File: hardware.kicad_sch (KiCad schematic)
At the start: 11 parts, among them J2 MDT320B03001, P1 USB_C_Plug, U4 CH340C

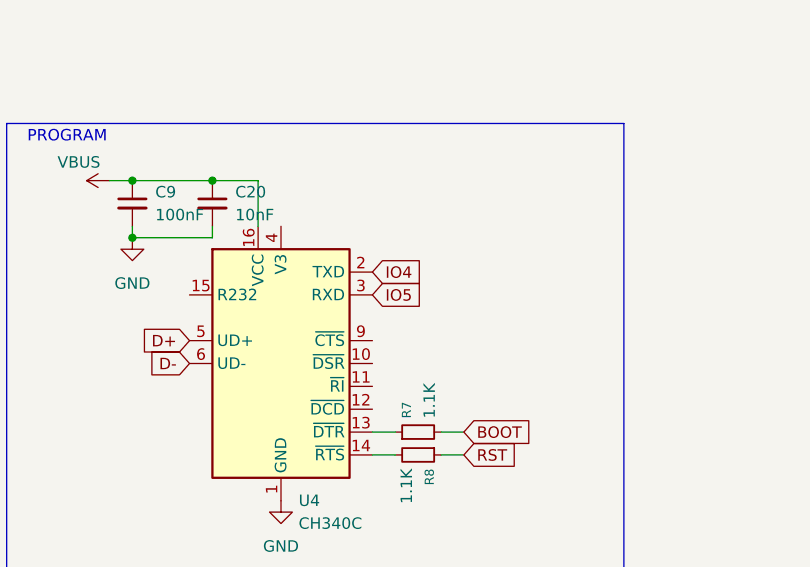
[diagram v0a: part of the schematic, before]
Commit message: switch uart wiring
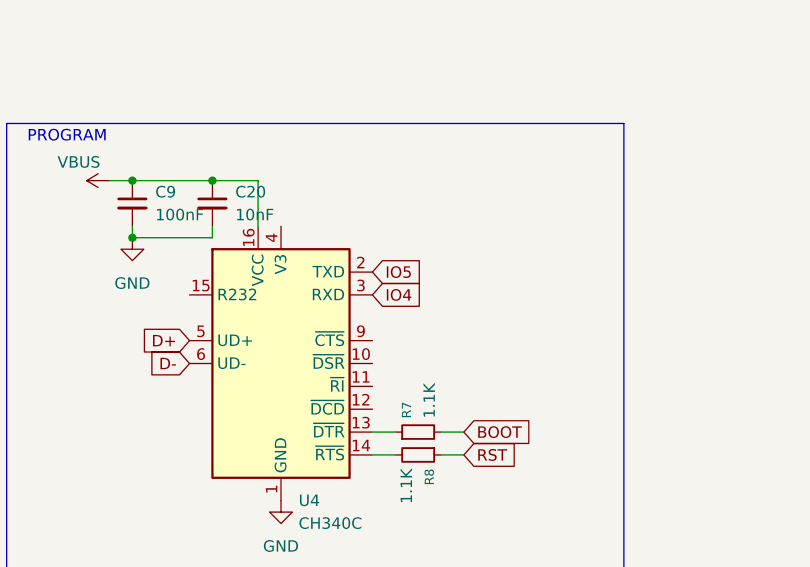
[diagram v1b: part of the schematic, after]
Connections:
- net IO4: now also U4.3 (RXD); no longer U4.2 (TXD)
- net IO5: now also U4.2 (TXD); no longer U4.3 (RXD)

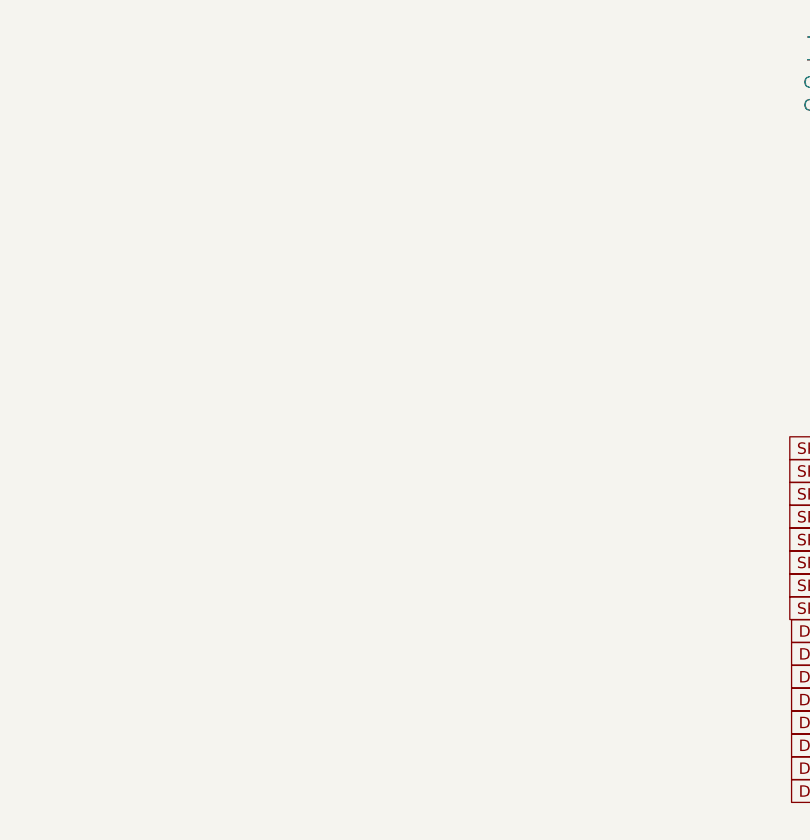
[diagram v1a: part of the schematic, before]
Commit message: add testing header
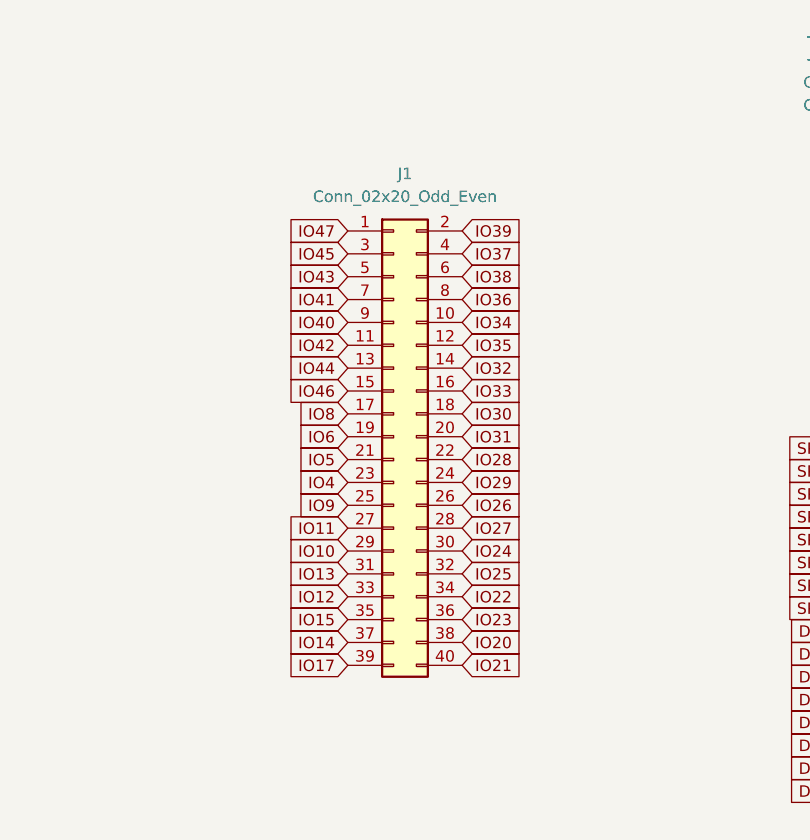
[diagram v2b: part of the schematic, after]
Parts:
- added J1: Conn_02x20_Odd_Even, Connector_IDC:IDC-Header_2x20_P2.54mm_Horizontal, symbol Connector_Generic:Conn_02x20_Odd_Even
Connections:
- net IO10: now also J1.29 (Pin_29)
- net IO11: now also J1.27 (Pin_27)
- net IO12: now also J1.33 (Pin_33)
- net IO13: now also J1.31 (Pin_31)
- net IO14: now also J1.37 (Pin_37)
- net IO15: now also J1.35 (Pin_35)
- net IO17: now also J1.39 (Pin_39)
- net IO20: now also J1.38 (Pin_38)
- net IO21: now also J1.40 (Pin_40)
- net IO22: now also J1.34 (Pin_34)
- net IO23: now also J1.36 (Pin_36)
- net IO24: now also J1.30 (Pin_30)
- net IO25: now also J1.32 (Pin_32)
- net IO26: now also J1.26 (Pin_26)
- net IO27: now also J1.28 (Pin_28)
- net IO28: now also J1.22 (Pin_22)
- net IO29: now also J1.24 (Pin_24)
- net IO30: now also J1.18 (Pin_18)
- net IO31: now also J1.20 (Pin_20)
- net IO32: now also J1.14 (Pin_14)
- net IO33: now also J1.16 (Pin_16)
- net IO34: now also J1.10 (Pin_10)
- net IO35: now also J1.12 (Pin_12)
- net IO36: now also J1.8 (Pin_8)
- net IO37: now also J1.4 (Pin_4)
- net IO38: now also J1.6 (Pin_6)
- net IO39: now also J1.2 (Pin_2)
- net IO4: now also J1.23 (Pin_23)
- net IO40: now also J1.9 (Pin_9)
- net IO41: now also J1.7 (Pin_7)
- net IO42: now also J1.11 (Pin_11)
- net IO43: now also J1.5 (Pin_5)
- net IO44: now also J1.13 (Pin_13)
- net IO45: now also J1.3 (Pin_3)
- net IO46: now also J1.15 (Pin_15)
- net IO47: now also J1.1 (Pin_1)
- net IO5: now also J1.21 (Pin_21)
- net IO6: now also J1.19 (Pin_19)
- net IO8: now also J1.17 (Pin_17)
- net IO9: now also J1.25 (Pin_25)

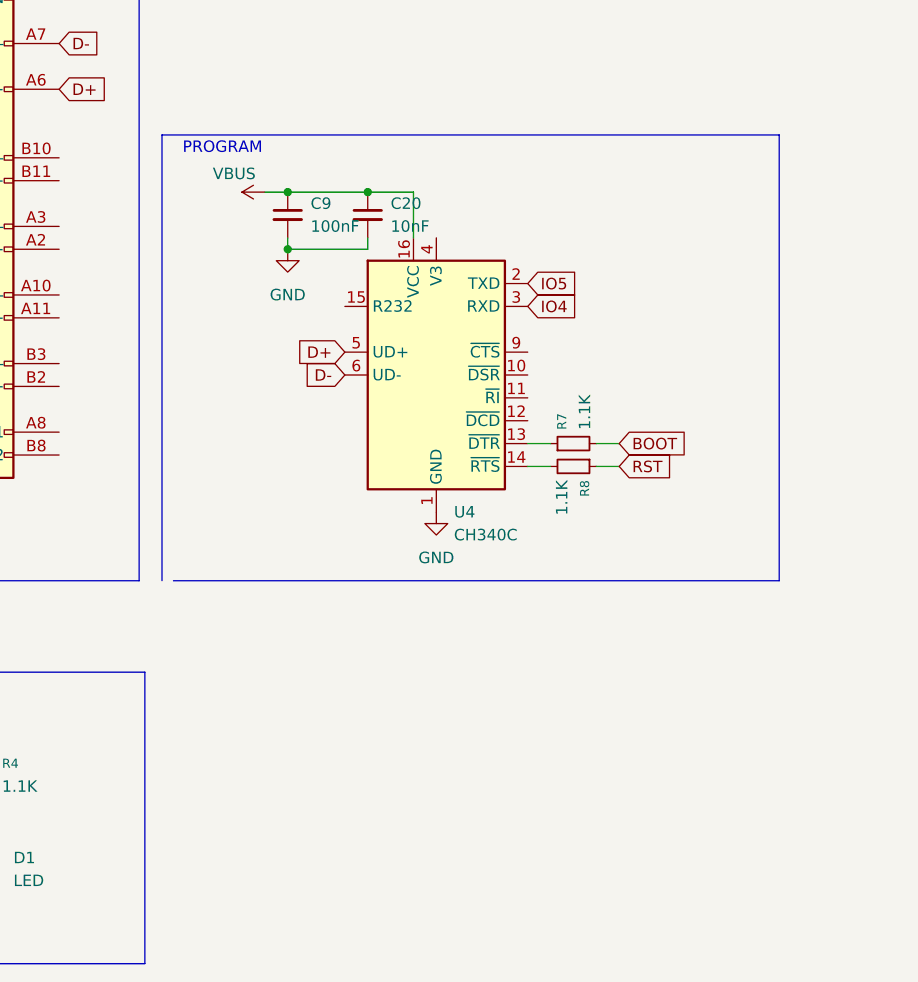
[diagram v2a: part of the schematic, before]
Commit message: add rst/boot pull up
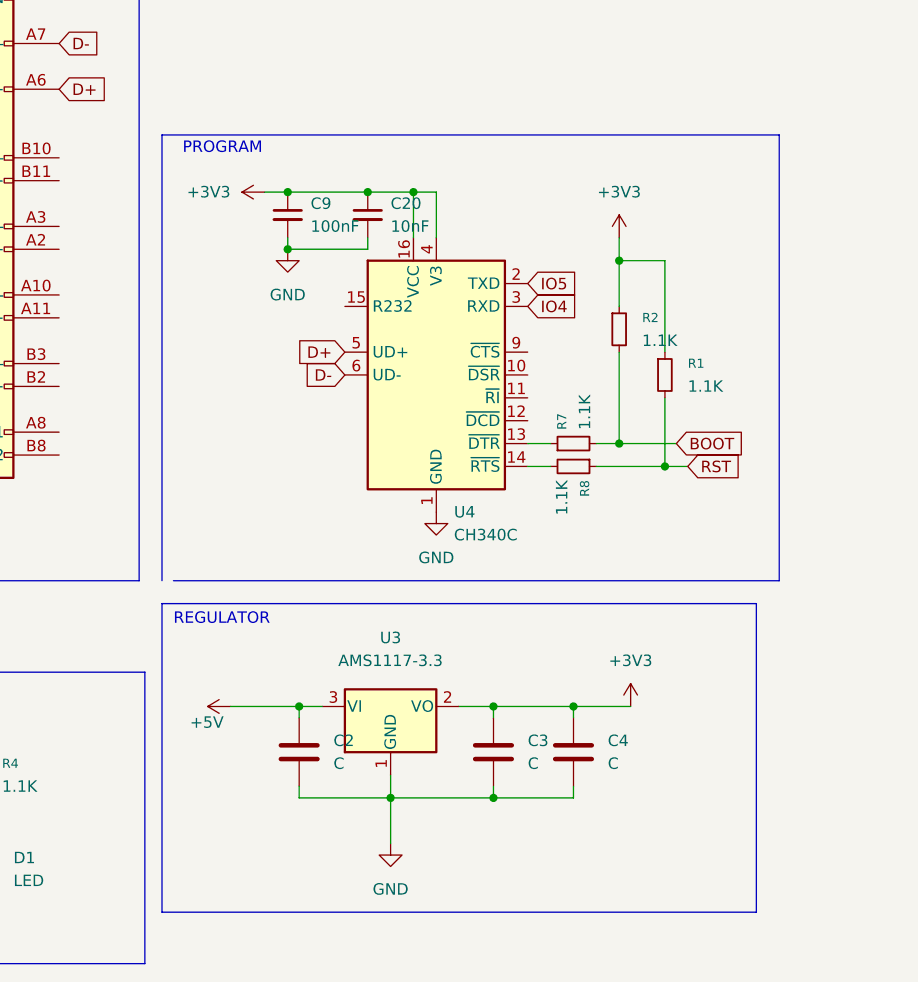
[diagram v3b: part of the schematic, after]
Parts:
- added C2, C3, C4: C, Capacitor_SMD:C_0603_1608Metric, symbol Device:C
- added R1, R2: 1.1K, Resistor_SMD:R_0603_1608Metric, symbol Device:R_Small
- added U3: AMS1117-3.3, Package_TO_SOT_SMD:SOT-223-3_TabPin2, symbol Regulator_Linear:AMS1117-3.3
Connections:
- net +5V: now also C2.1, U3.3 (VI); no longer C20.1, C9.1, U4.16 (VCC)
- net BOOT: now also R2.2
- net GND: now also C2.2, C3.2, C4.2, U3.1 (GND)
- net RST: now also R1.2
- net +3V3: now reaches U4.4 (V3)
- net +3V3: now also C20.1, C9.1, U4.16 (VCC), C3.1, C4.1, R1.1, R2.1, U3.2 (VO)
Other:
- note added: "REGULATOR"

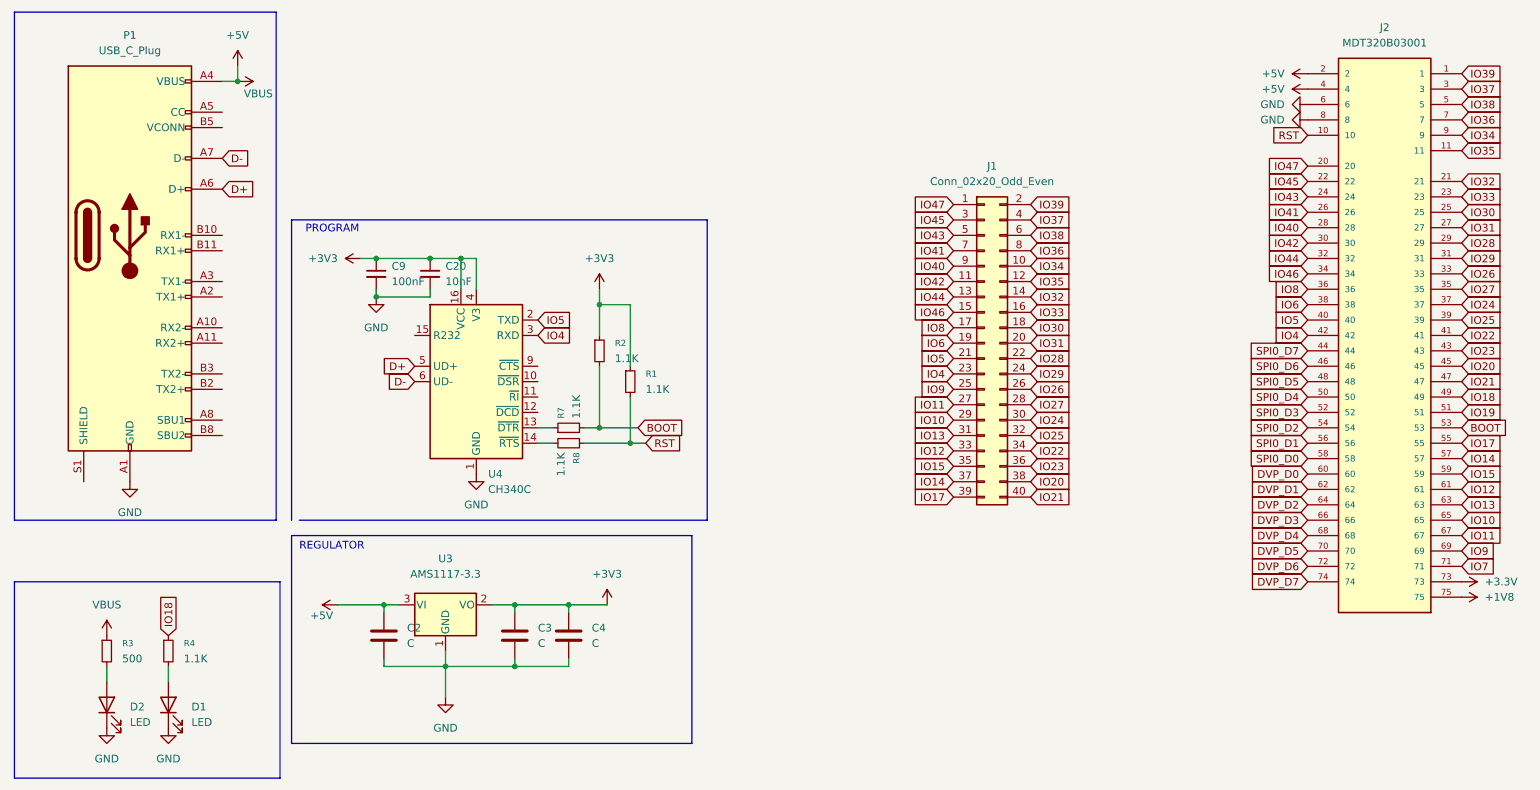
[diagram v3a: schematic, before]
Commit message: fix usb c wiring
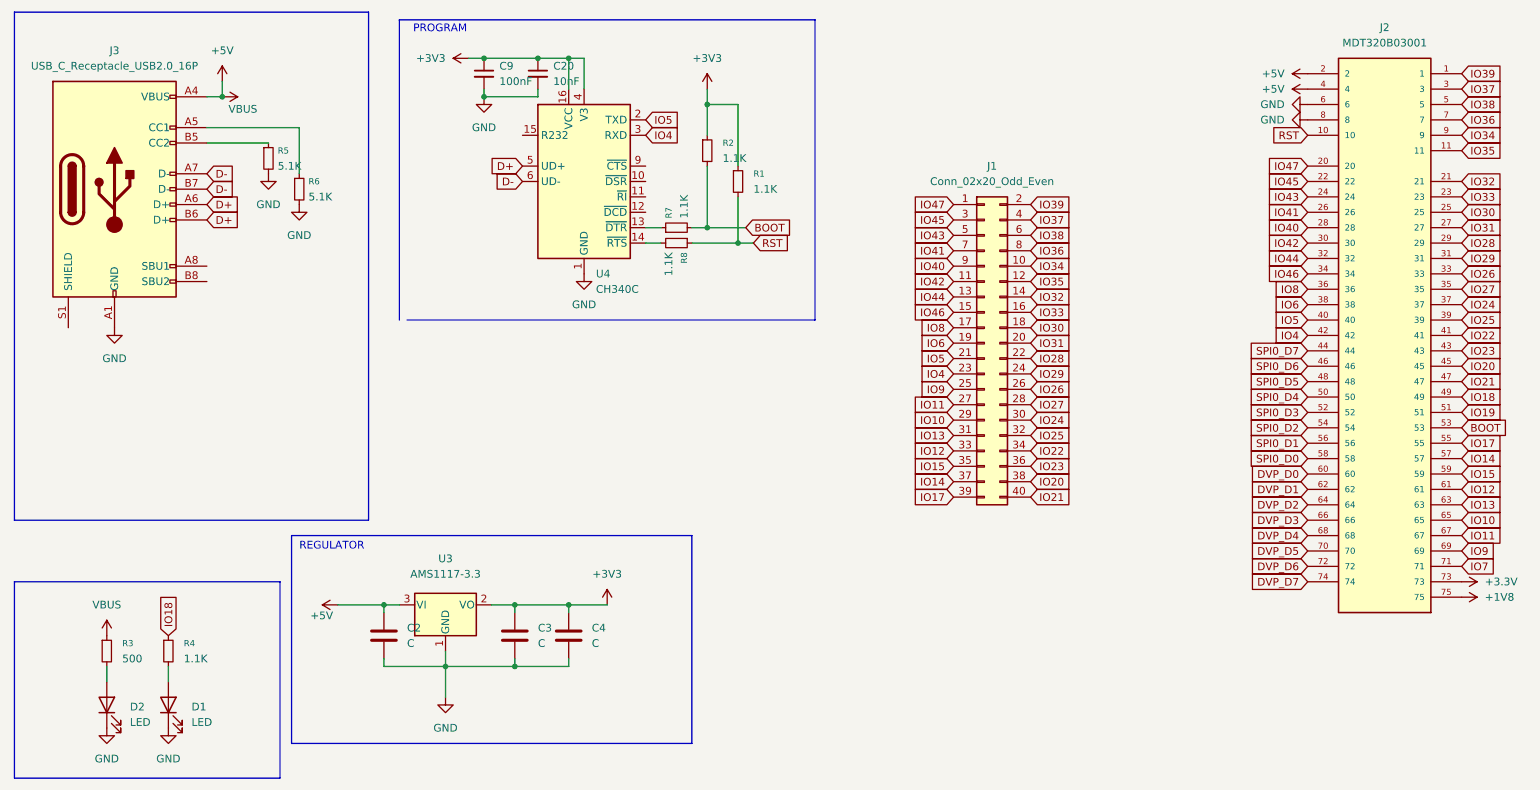
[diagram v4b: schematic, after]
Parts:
- removed P1: USB_C_Plug, Connector_USB:USB_C_Receptacle_GCT_USB4105-xx-A_16P_TopMnt_Horizontal, symbol Connector:USB_C_Plug
- added J3: USB_C_Receptacle_USB2.0_16P, symbol Connector:USB_C_Receptacle_USB2.0_16P
- added R5, R6: 5.1K, Resistor_SMD:R_0603_1608Metric, symbol Device:R_Small
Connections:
- net +5V: now also J3.A4 (VBUS), J3.A9 (VBUS), J3.B4 (VBUS), J3.B9 (VBUS)
- net D+: now also J3.A6 (D+), J3.B6 (D+)
- net D-: now also J3.A7 (D-), J3.B7 (D-)
- net GND: now also J3.A1 (GND), J3.A12 (GND), J3.B1 (GND), J3.B12 (GND), R5.2, R6.2
- new net: J3.B5 (CC2), R5.1
- new net: J3.A5 (CC1), R6.1
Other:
- moved on the sheet: C20, C9, R1, R2, R7, R8, U4
